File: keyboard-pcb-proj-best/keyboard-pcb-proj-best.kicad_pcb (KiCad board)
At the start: 2 copper layers, 76.2 x 38.1 mm, 24 parts, among them SW1 SW_PUSH, U1 ATmega32U4-A, Y1 16Mhz

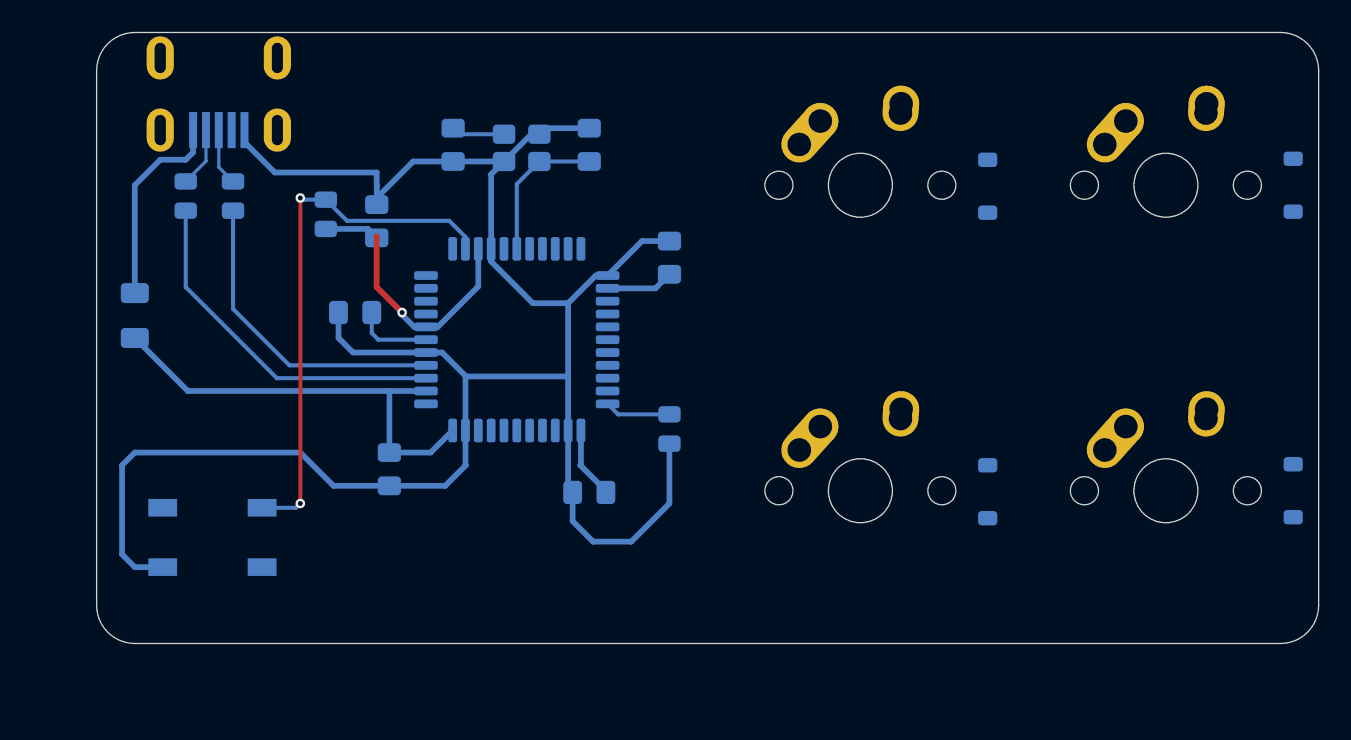
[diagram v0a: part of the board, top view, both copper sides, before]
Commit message: Finalized Rerouting
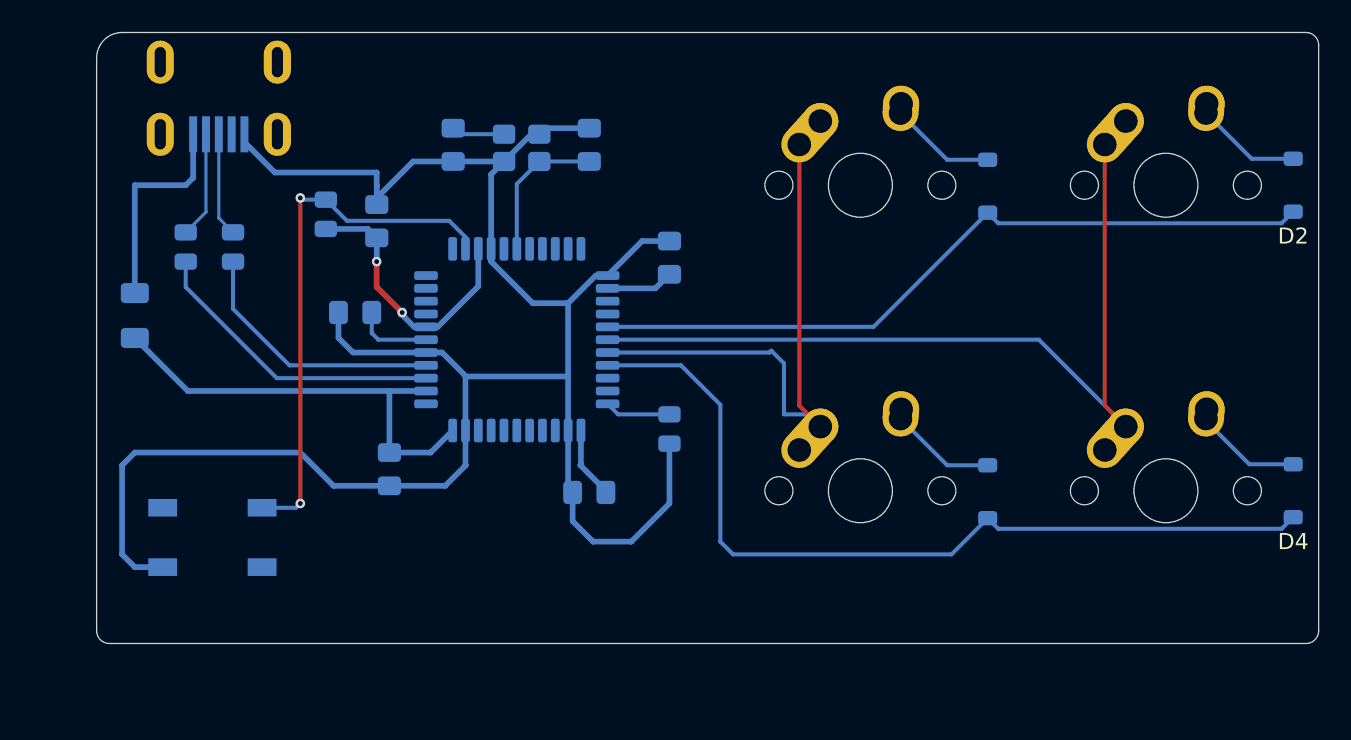
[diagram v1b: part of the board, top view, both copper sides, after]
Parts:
- moved R2 3.17 mm to (176.0, 46.7)
- moved R3 3.17 mm to (173.0, 46.7)
- moved USB1 0.26 mm to (175.1, 35.2)
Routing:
- net ROW1: track 0.00 -> 54.1 mm
- net COL1: track 0.00 -> 52.7 mm
- net ROW0: track 0.00 -> 46.3 mm
- net COL0: track 0.00 -> 35.3 mm
- net Net-(D4-A): track 0.00 -> 6.70 mm
- net Net-(D3-A): track 0.00 -> 6.64 mm
- net Net-(D1-A): track 0.00 -> 6.64 mm
- net Net-(D2-A): track 0.00 -> 6.62 mm
- net Net-(U1-D-): track 22.1 -> 18.9 mm
- net Net-(U1-D+): track 19.6 -> 16.4 mm
- net D-: track 3.72 -> 6.64 mm
- net D+: track 3.57 -> 6.48 mm
- net VCC: track 12.6 -> 13.3 mm
- net +5V: track 54.0 -> 53.9 mm, vias 1 -> 2
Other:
- outline, holes or cut-outs redrawn
